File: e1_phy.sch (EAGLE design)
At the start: 126 parts, among them IC2 LD117AS33TR, IC3 LD117AS33TR, U1 IDT82V2081, U2 GPS_GNS_2201, U3 VCTCXO-CONNORWINFIELD, U4 VCXO_TAITIEN_VT, U5 IP4234CZ6, X2 SMA-142-0701-801/806, X3 JACK2.5_SJ-2523, X4 0446200002

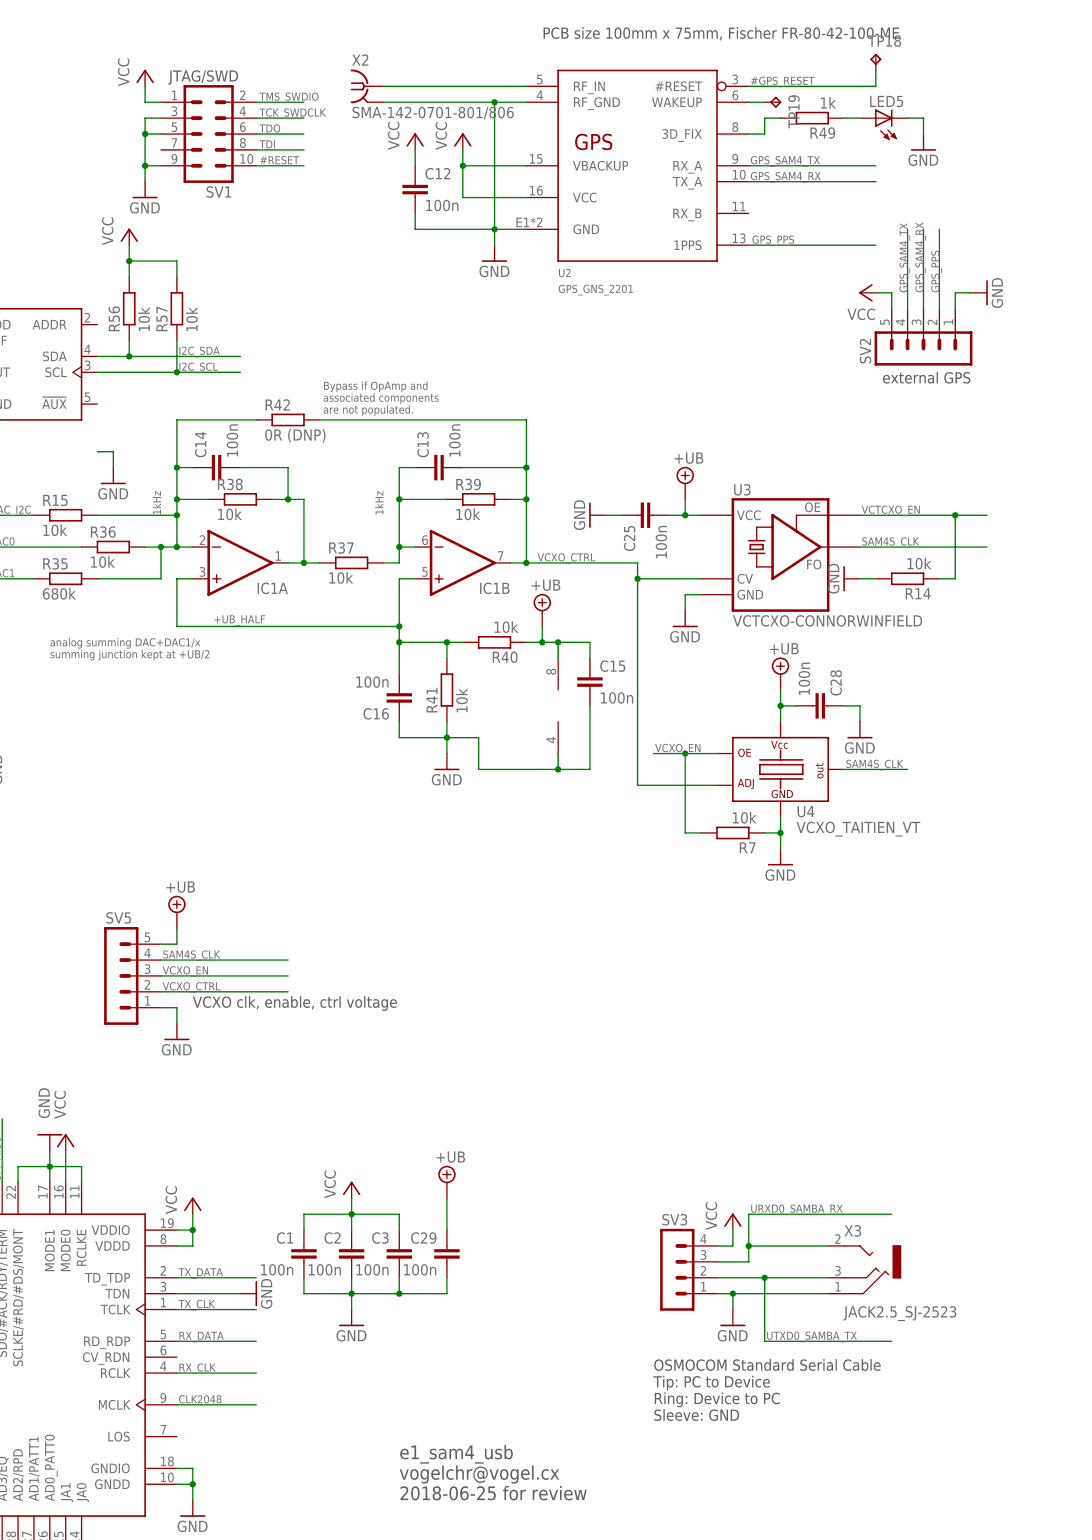
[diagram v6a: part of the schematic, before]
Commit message: More review comments implemented.
Done:
 - ESD protection on UART
 - changed JTAG to 2x10 standard ARM (but only minimal usage of pins on
	 SAM4S)
 - FTDI pinout on serial port header
 - LEDS moved near frontpanel, maybe later exchange by side-emitting
   type

Refused:
 - change R on LEDs (can change later if too dim)
 - termination on GPS rx/tx/pp
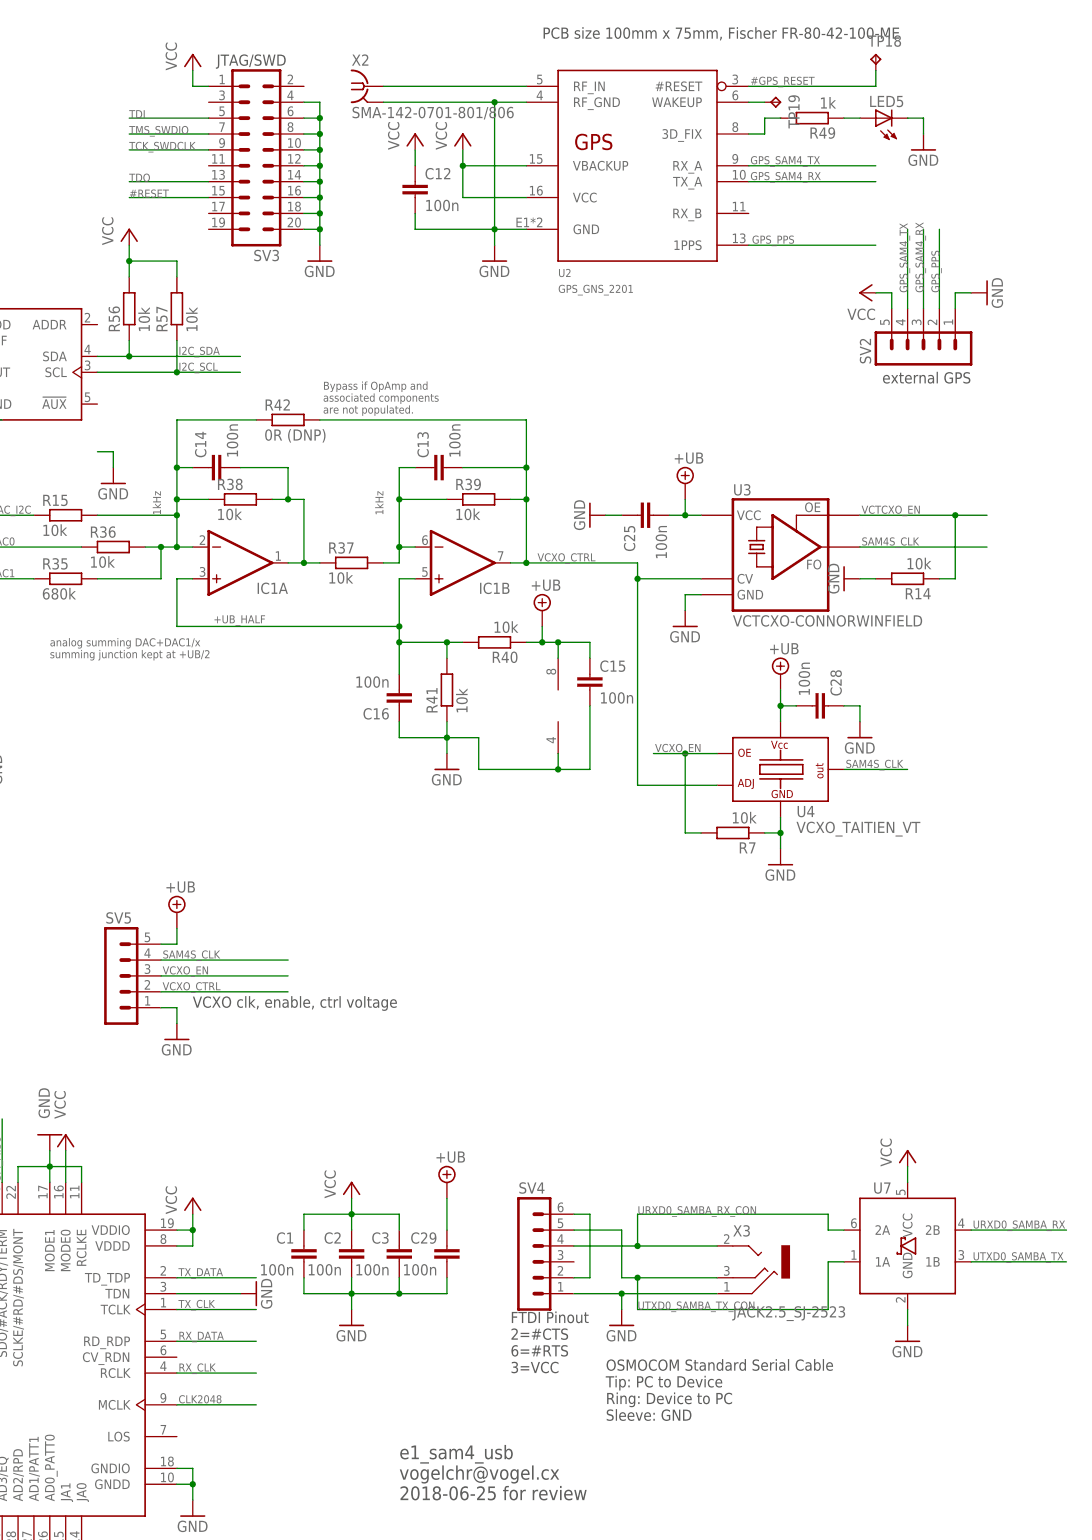
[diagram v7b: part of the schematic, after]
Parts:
- removed SV1: (no value), con-lstb:MA05-2
- added SV4: (no value), con-lstb:MA06-1
- added U7: IP4234CZ6, laforge:IP4234CZ6
- SV3: device con-lstb:MA04-1 -> con-lstb:MA10-2
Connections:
- new net N$32: SV4.2, SV4.6
- new net URXD0_SAMBA_RX_CON: SV4.4, U7.2A, X3.TIP
- new net UTXD0_SAMBA_TX_CON: SV4.5, U7.1A, X3.MIDDLE
- net #RESET: now also SV3.15; no longer SV1.10
- net GND: now also SV3.10, SV3.12, SV3.14, SV3.16, SV3.18, SV3.20, SV3.4, SV3.6, SV3.8, SV4.1, U7.GND; no longer SV1.3, SV1.5, SV1.9, SV3.1
- net TCK_SWDCLK: now also SV3.9; no longer SV1.4
- net TDI: now also SV3.5; no longer SV1.8
- net TDO: now also SV3.13; no longer SV1.6
- net TMS_SWDIO: now also SV3.7; no longer SV1.2
- net URXD0_SAMBA_RX: now also U7.2B; no longer SV3.3, X3.TIP
- net UTXD0_SAMBA_TX: now also U7.1B; no longer SV3.2, X3.MIDDLE
- net VCC: now also SV3.1, U7.VCC; no longer SV1.1, SV3.4
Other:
- note added: "FTDI Pinout 2=#CTS 6=#RTS 3=VCC"
- moved on the sheet: X3

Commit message: Implementing further review comments:
* SPI/I2C header UEXT compatible 2x5
* Pullups on #RESET & JTAG TCK, TMS = SWDIO, SWCK
* Pullup on UART RX
* Pullup on Liu #RST
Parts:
- removed R56, R57: 10k, rcl:R-EU_R0603
- removed SV6: (no value), con-lstb:MA05-2
- added RN3, RN4: 10k, resistor-dil:4R-NEXB38V
- added SV1: (no value), con-lstb:MA05-2
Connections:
- net #RESET: now also RN4D.1
- net #RST_LIU: now also R11.1
- net #SPI_CS0: now also RN3B.1, SV1.10; no longer R10.1, SV6.5
- net #SPI_CS2: now also RN3D.1, SV1.4; no longer R11.1, SV6.6
- net GND: now also SV1.2; no longer SV6.2, SV6.9
- net I2C_SCL: now also RN3C.1, SV1.5; no longer R57.1, SV6.8
- net I2C_SDA: now also RN3A.1, SV1.6; no longer R56.1, SV6.7
- net SPI_MISO: now also SV1.7; no longer SV6.3
- net SPI_MOSI: now also SV1.8; no longer SV6.4
- net SPI_SCK: now also SV1.9; no longer SV6.1
- net TCK_SWDCLK: now also RN4B.1
- net TMS_SWDIO: now also RN4A.1
- net URXD0_SAMBA_RX_CON: now also R10.1
- net VCC: now also RN3A.2, RN3B.2, RN3C.2, RN3D.2, RN4A.2, RN4B.2, RN4C.2, RN4D.2, SV1.1; no longer R56.2, R57.2, SV6.10
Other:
- note added: "Power LEDs"
- note added: "UEXT 4="TxD"=#CS2"
- note removed: "SPI and I2C"
- moved on the sheet: C1, C2, C29, C3, LED3, LED4, LED6, LED7, LED8, R10, R11, R47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
